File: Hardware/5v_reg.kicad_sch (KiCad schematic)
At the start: 7 parts, among them U2 TPS54302

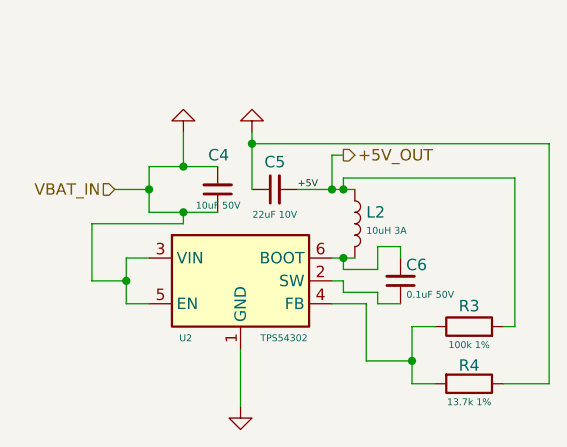
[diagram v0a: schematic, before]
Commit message: Finalize schematic: Add connectors, LEDs, Buzzer and fix all ERC errors
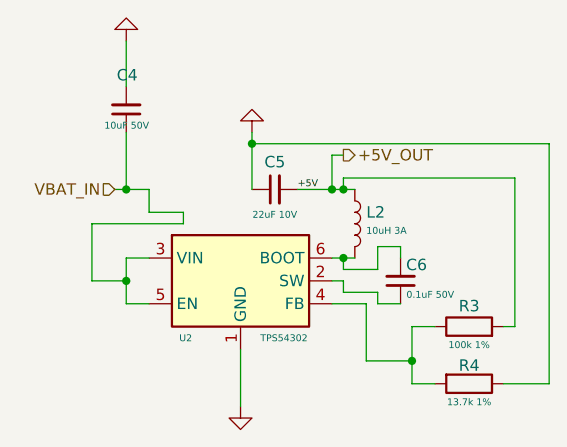
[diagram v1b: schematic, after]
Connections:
- net GND: no longer C4.1, U2.3 (VIN), U2.5 (EN)
- new net VBAT_IN: C4.1, U2.3 (VIN), U2.5 (EN)
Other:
- moved on the sheet: C4
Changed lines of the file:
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@@
 	(paper "A4")
+	(junction
+		(at 129.54 90.17)
+		(diameter 0)
+		(color 0 0 0 0)
+	)
 	(junction
 		(at 143.51 85.09)
@@
 	)
 	(junction
-		(at 132.08 90.17)
-		(diameter 0)
-		(color 0 0 0 0)
-	)
-	(junction
-		(at 135.89 87.63)
-		(diameter 0)
-		(color 0 0 0 0)
-	)
-	(junction
 		(at 153.67 97.79)
 		(diameter 0)
@@
 	)
 	(junction
-		(at 135.89 92.71)
-		(diameter 0)
-		(color 0 0 0 0)
-	)
-	(junction
 		(at 129.54 100.33)
 		(diameter 0)
@@
 	(wire
 		(pts
-			(xy 128.27 90.17) (xy 132.08 90.17)
+			(xy 128.27 90.17) (xy 129.54 90.17)
 		)
 		(stroke
@@
 	(wire
 		(pts
+			(xy 129.54 90.17) (xy 132.08 90.17)
+		)
+		(stroke
+			(width 0)
+			(type default)
+		)
+	)
+	(wire
+		(pts
 			(xy 157.48 101.6) (xy 153.67 101.6)
 		)
@@
 	(wire
 		(pts
+			(xy 129.54 83.82) (xy 129.54 90.17)
+		)
+		(stroke
+			(width 0)
+			(type default)
+		)
+	)
+	(wire
+		(pts
 			(xy 153.67 101.6) (xy 153.67 100.33)
 		)
@@
 	(wire
 		(pts
-			(xy 135.89 87.63) (xy 139.7 87.63)
-		)
-		(stroke
-			(width 0)
-			(type default)
-		)
-	)
-	(wire
-		(pts
-			(xy 132.08 87.63) (xy 135.89 87.63)
+			(xy 129.54 73.66) (xy 129.54 78.74)
 		)
 		(stroke
@@
 	(wire
 		(pts
-			(xy 135.89 83.82) (xy 135.89 87.63)
-		)
-		(stroke
-			(width 0)
-			(type default)
-		)
-	)
-	(wire
-		(pts
 			(xy 143.51 83.82) (xy 143.51 85.09)
 		)
@@
 	(wire
 		(pts
-			(xy 139.7 92.71) (xy 135.89 92.71)
-		)
-		(stroke
-			(width 0)
-			(type default)
-		)
-	)
-	(wire
-		(pts
 			(xy 157.48 102.87) (xy 157.48 101.6)
 		)
@@
 		(pts
 			(xy 156.21 109.22) (xy 156.21 102.87)
-		)
-		(stroke
-			(width 0)
-			(type default)
-		)
-	)
-	(wire
-		(pts
-			(xy 132.08 87.63) (xy 132.08 90.17)
 		)
 		(stroke
@@
 	)
 	(symbol
-		(lib_id "power:GND")
-		(at 135.89 83.82 180)
-		(unit 1)
-		(exclude_from_sim no)
-		(in_bom yes)
-		(on_board yes)
-		(dnp no)
-		(fields_autoplaced yes)
-		(property "Reference" "#PWR04"
-			(at 135.89 77.47 0)
-			(effects
-				(font
-					(size 1.27 1.27)
-				)
-				(hide yes)
-			)
-		)
-		(property "Value" "GND"
-			(at 135.89 78.74 0)
-			(effects
-				(font
-					(size 1.27 1.27)
-				)
-				(hide yes)
-			)
-		)
-		(property "Footprint" ""
-			(at 135.89 83.82 0)
-			(effects
-				(font
-					(size 1.27 1.27)
-				)
-				(hide yes)
-			)
-		)
-		(property "Datasheet" ""
-			(at 135.89 83.82 0)
-			(effects
-				(font
-					(size 1.27 1.27)
-				)
-				(hide yes)
-			)
-		)
-		(property "Description" "Power symbol creates a global label with name \"GND\" , ground"
-			(at 135.89 83.82 0)
-			(effects
-				(font
-					(size 1.27 1.27)
-				)
-				(hide yes)
-			)
-		)
-		(pin "1"
-		)
-		(instances
-			(project "fligh controler"
-				(path "/9ac87d7b-7c63-4195-8fde-46e8d8136fbe/cb72bb9b-4878-4d82-89eb-a84c13808311/f284c435-5dcc-4621-98e9-3353b10102f5"
-					(reference "#PWR04")
-					(unit 1)
-				)
-			)
-		)
-	)
-	(symbol
 		(lib_id "Device:L")
 		(at 154.94 93.98 0)
@@
 	)
 	(symbol
+		(lib_id "power:GND")
+		(at 129.54 73.66 180)
+		(unit 1)
+		(exclude_from_sim no)
+		(in_bom yes)
+		(on_board yes)
+		(dnp no)
+		(fields_autoplaced yes)
+		(property "Reference" "#PWR040"
+			(at 129.54 67.31 0)
+			(effects
+				(font
+					(size 1.27 1.27)
+				)
+				(hide yes)
+			)
+		)
+		(property "Value" "GND"
+			(at 129.54 68.58 0)
+			(effects
+				(font
+					(size 1.27 1.27)
+				)
+				(hide yes)
+			)
+		)
+		(property "Footprint" ""
+			(at 129.54 73.66 0)
+			(effects
+				(font
+					(size 1.27 1.27)
+				)
+				(hide yes)
+			)
+		)
+		(property "Datasheet" ""
+			(at 129.54 73.66 0)
+			(effects
+				(font
+					(size 1.27 1.27)
+				)
+				(hide yes)
+			)
+		)
+		(property "Description" "Power symbol creates a global label with name \"GND\" , ground"
+			(at 129.54 73.66 0)
+			(effects
+				(font
+					(size 1.27 1.27)
+				)
+				(hide yes)
+			)
+		)
+		(pin "1"
+		)
+		(instances
+			(project "fligh controler"
+				(path "/9ac87d7b-7c63-4195-8fde-46e8d8136fbe/cb72bb9b-4878-4d82-89eb-a84c13808311/f284c435-5dcc-4621-98e9-3353b10102f5"
+					(reference "#PWR040")
+					(unit 1)
+				)
+			)
+		)
+	)
+	(symbol
 		(lib_id "Regulator_Switching:TPS54302")
 		(at 142.24 100.33 0)
@@
 	(symbol
 		(lib_id "Device:C_Small")
-		(at 139.7 90.17 180)
+		(at 129.54 81.28 180)
 		(unit 1)
 		(exclude_from_sim no)
@@
 		(fields_autoplaced yes)
 		(property "Reference" "C4"
-			(at 140.97 86.36 0)
+			(at 130.81 77.47 0)
 			(effects
 				(font
@@
 		)
 		(property "Value" "10uF 50V"
-			(at 142.24 91.948 0)
+			(at 132.08 83.058 0)
 			(effects
 				(font
@@
 		)
 		(property "Footprint" ""
-			(at 139.7 90.17 0)
+			(at 129.54 81.28 0)
 			(effects
 				(font
@@
 		)
 		(property "Datasheet" "~"
-			(at 139.7 90.17 0)
+			(at 129.54 81.28 0)
 			(effects
 				(font
@@
 		)
 		(property "Description" "Unpolarized capacitor, small symbol"
-			(at 139.7 90.17 0)
-			(effects
-				(font
+			(at 129.54 81.28 0)
+			(effects
+				(font

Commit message: Update schematic: Add SDIO Blackbox, ESC Redundancy and remove UART5
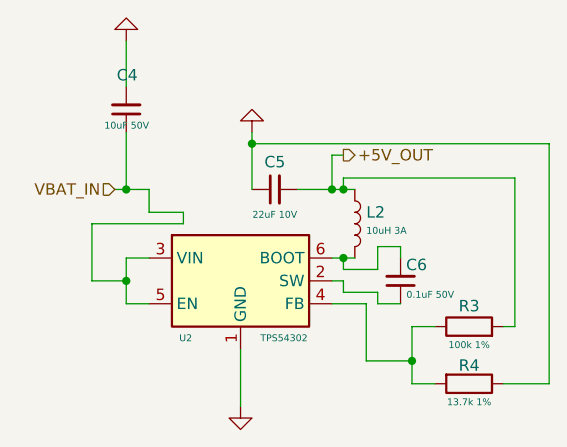
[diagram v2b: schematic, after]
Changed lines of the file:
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@@
-		)
-	)
-	(label "+5V"
-		(at 148.59 90.17 0)
-		(effects
-			(font
-				(size 0.762 0.762)
-			)
-			(justify left bottom)
 		)
 	)

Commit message: Finalize component placement and silkscreen
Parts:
- C4, C5: footprint (none) -> Capacitor_SMD:C_0805_2012Metric
- C6: footprint (none) -> Capacitor_SMD:C_0402_1005Metric
- L2: footprint (none) -> Inductor_SMD:L_Taiyo-Yuden_NR-40xx
- R3, R4: footprint (none) -> Resistor_SMD:R_0402_1005Metric
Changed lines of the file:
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@@
 			)
 		)
-		(property "Footprint" ""
+		(property "Footprint" "Capacitor_SMD:C_0805_2012Metric"
 			(at 146.05 90.17 0)
 			(effects
@@
 			)
 		)
-		(property "Footprint" ""
+		(property "Footprint" "Resistor_SMD:R_0402_1005Metric"
 			(at 167.64 107.188 90)
 			(effects
@@
 			)
 		)
-		(property "Footprint" ""
+		(property "Footprint" "Capacitor_SMD:C_0402_1005Metric"
 			(at 160.02 100.33 0)
 			(effects
@@
 			)
 		)
-		(property "Footprint" ""
+		(property "Footprint" "Resistor_SMD:R_0402_1005Metric"
 			(at 167.64 109.982 90)
 			(effects
@@
 			)
 		)
-		(property "Footprint" ""
+		(property "Footprint" "Inductor_SMD:L_Taiyo-Yuden_NR-40xx"
 			(at 154.94 93.98 0)
 			(effects
@@
 			)
 		)
-		(property "Footprint" ""
+		(property "Footprint" "Capacitor_SMD:C_0805_2012Metric"
 			(at 129.54 81.28 0)
 			(effects
